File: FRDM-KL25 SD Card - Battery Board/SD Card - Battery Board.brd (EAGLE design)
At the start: 81.3 x 53.3 mm, 64 parts, among them J3 SSW-108-02-S-D, J4 SSW-110-02-S-D, J5 SSW-108-02-S-D, J6 SSW-106-02-S-D, U1 TPS63001, U2 TPS63002, U3 BQ27510DRZT-G3, U4 BQ24210DQCT

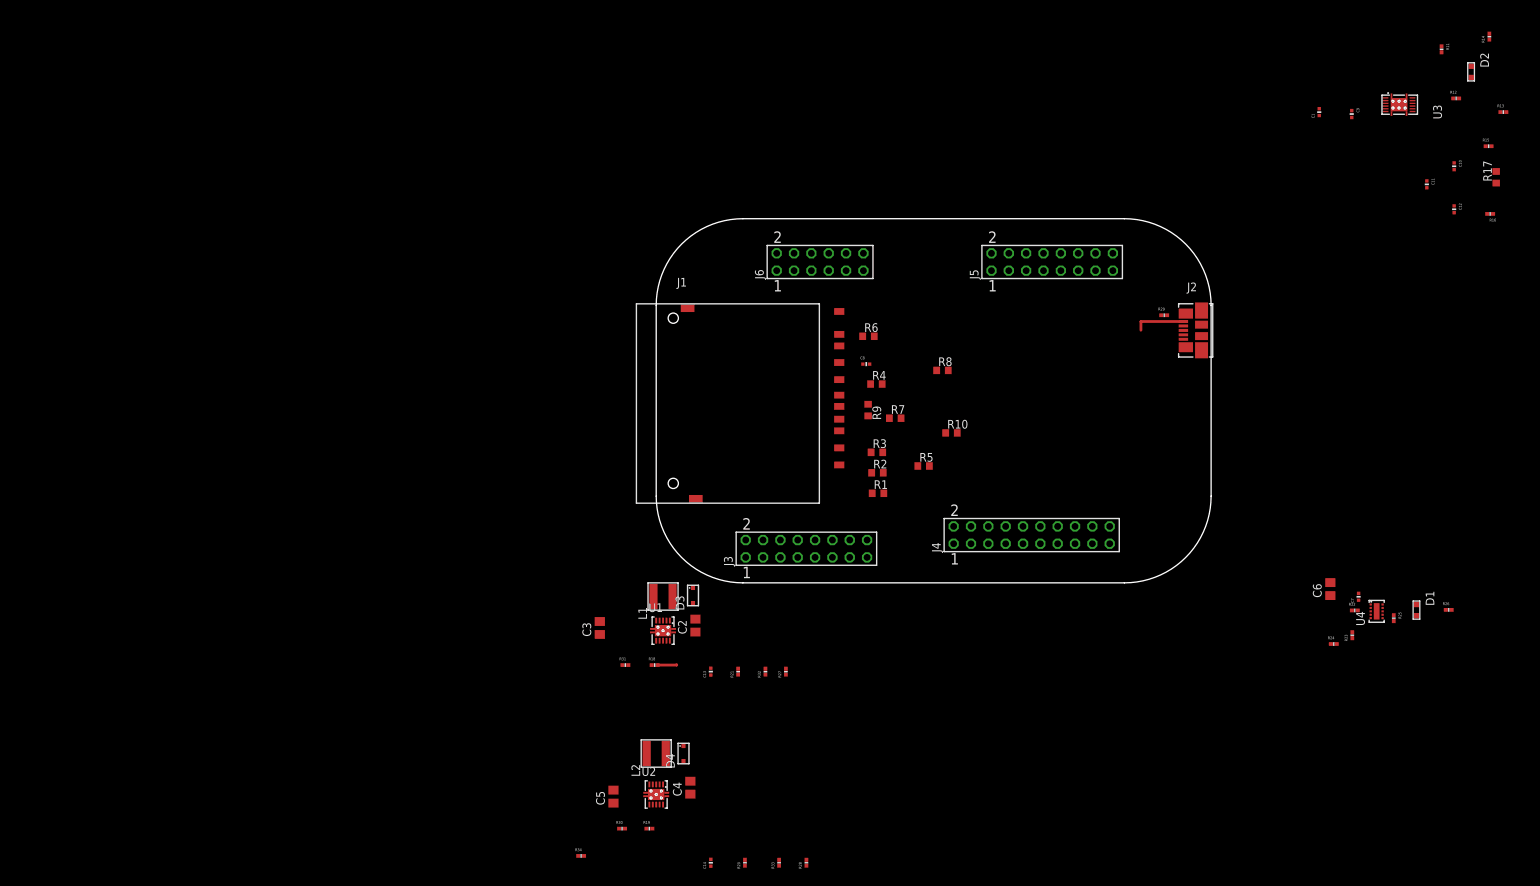
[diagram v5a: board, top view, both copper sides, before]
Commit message: FRDM-KL25Z: Grouped and positioned componets now that all are using 0402 corrected packages to be 0402 and rearanged compoinets to better fit space allowed by the PCB
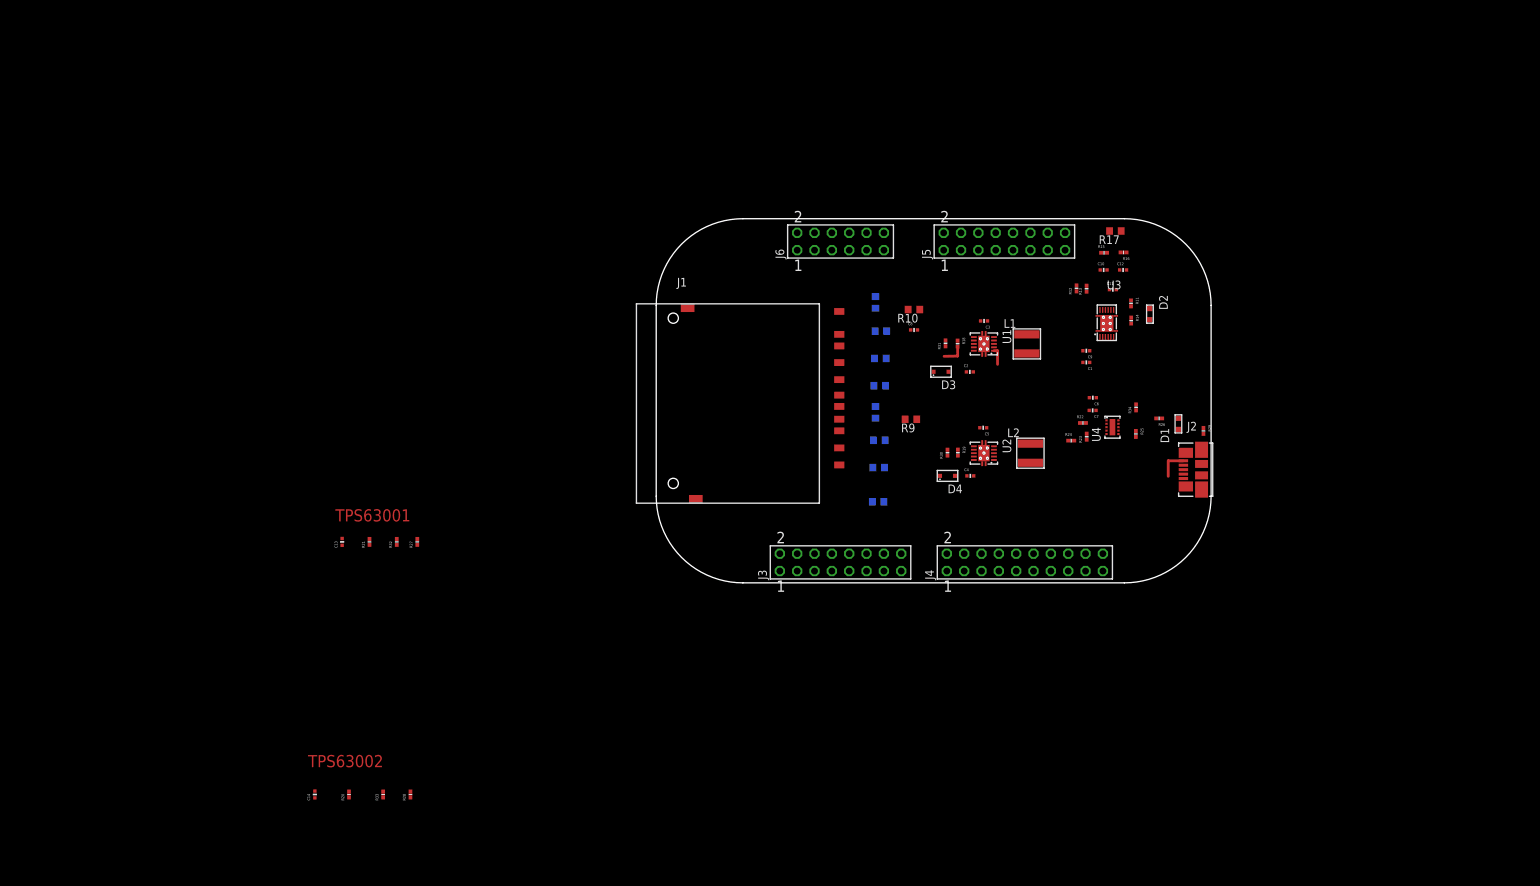
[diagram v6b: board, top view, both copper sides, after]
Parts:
- C2, C3, C4, C5, C6: device Kas-Capacitors:C0805 -> Kas-Capacitors:C0402
- moved R34 104.5 mm to (70.3, 25.7), turned to 90 degrees
- moved C5 76.5 mm to (47.9, 22.7), turned to 180 degrees
- moved R30 72.8 mm to (42.7, 19.1), turned to 90 degrees
- moved C3 72.0 mm to (48.0, 38.4), turned to 180 degrees
- moved R19 71.2 mm to (44.2, 19.1), turned to 270 degrees
- moved L2 70.3 mm to (54.8, 19.0), turned to 180 degrees
- moved U2 69.3 mm to (48.0, 19.0), turned to 90 degrees
- moved R14 67.0 mm to (69.6, 38.4), turned to 270 degrees
- moved R31 66.5 mm to (42.4, 35.1), turned to 90 degrees
- moved R13 66.3 mm to (63.0, 43.1), turned to 90 degrees
- moved L1 64.9 mm to (54.3, 35.0), turned to 180 degrees
- moved R18 64.7 mm to (44.1, 35.0), turned to 270 degrees
- moved U1 63.0 mm to (48.0, 35.0), turned to 90 degrees
- moved R12 62.2 mm to (61.6, 43.1), turned to 90 degrees
- moved C4 61.4 mm to (46.0, 15.7), turned to 0 degrees
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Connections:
- removed net N$12: C5.1, U2.P$5
- net GND: now also R29.1
- net N$28: now also J2.P$11; no longer J2.P$6
- net PACK+: now also C5.1, U2.P$5
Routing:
- net GND: track 7.50 -> 4.50 mm
- net VCC: track 0.00 -> 2.52 mm
- net PACK+: track 2.84 -> 3.41 mm
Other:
- board text added: "TPS63001"
- board text added: "TPS63002"

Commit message: FRDM-KL25Z: Fixed baord outline to matxh with Freescales coordinate system. Placed connectors as per Freescales placement file and replaced all previous components on board in the correct orientation. On the schematics the USB connetor was moved from sheet 2 to sheet 3 with all the other connectors.
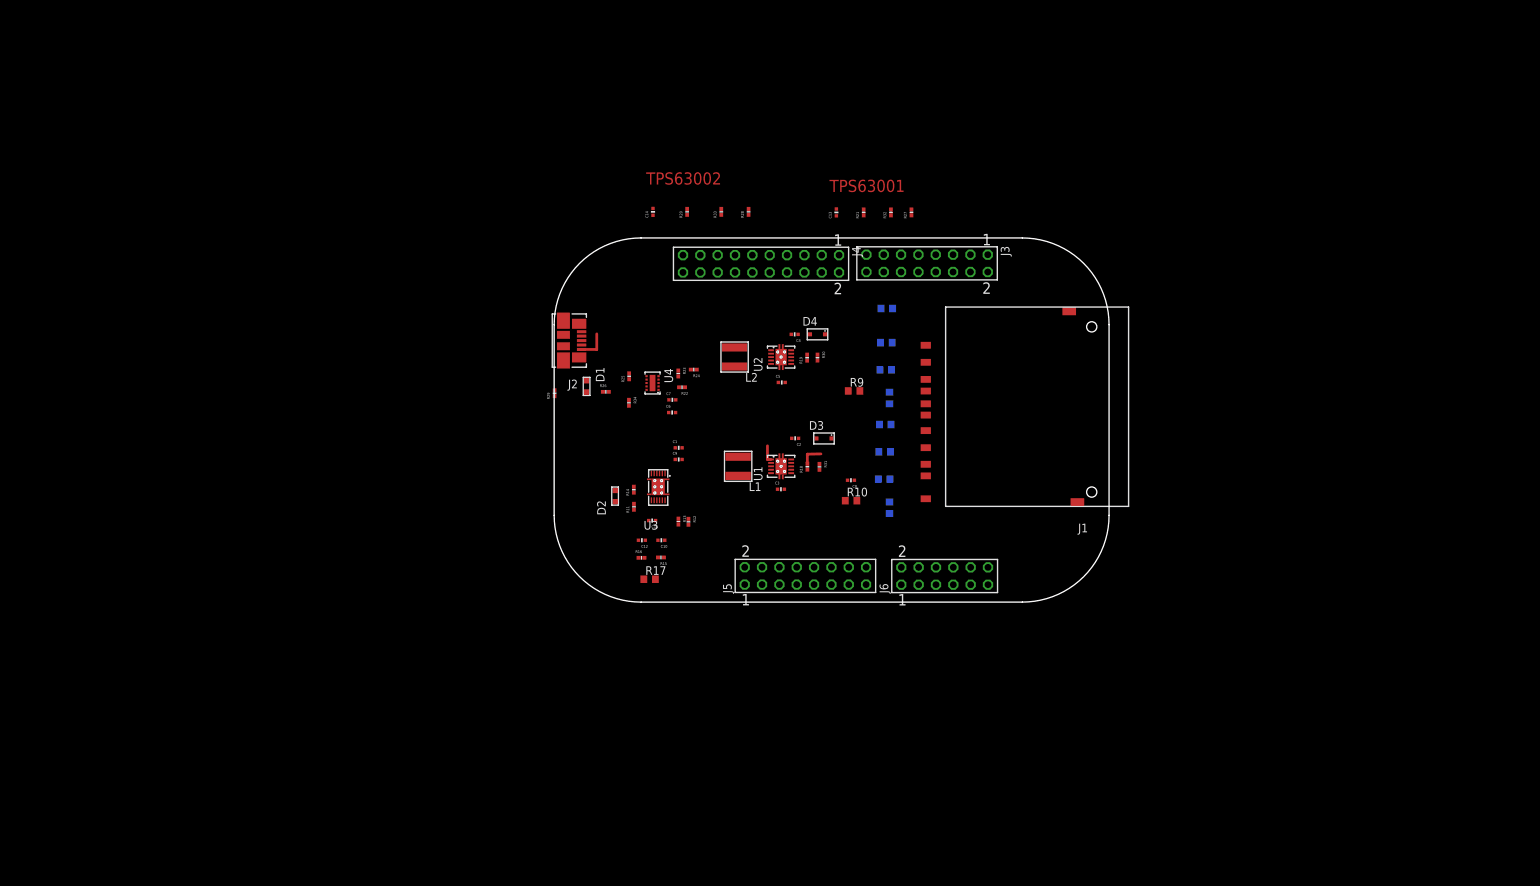
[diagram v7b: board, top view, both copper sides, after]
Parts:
- moved C14 98.7 mm to (-0.47, 54.3)
- moved R20 98.7 mm to (4.53, 54.3)
- moved R28 98.7 mm to (13.5, 54.3)
- moved R33 98.7 mm to (9.53, 54.3)
- moved R29 95.2 mm to (-14.9, 27.8), turned to 90 degrees
- moved J2 90.2 mm to (-10.9, 35.5), turned to 0 degrees
- moved C13 87.0 mm to (26.4, 54.3)
- moved R21 87.0 mm to (30.4, 54.3)
- moved R27 87.0 mm to (37.4, 54.3)
- moved R32 87.0 mm to (34.4, 54.3)
- moved D1 86.9 mm to (-10.2, 28.8), turned to 90 degrees
- moved R17 85.2 mm to (-0.97, 0.53), turned to 0 degrees
- moved R16 83.6 mm to (-2.16, 3.67), turned to 0 degrees
- moved D2 82.8 mm to (-6.03, 12.7), turned to 270 degrees
- moved R26 81.1 mm to (-7.38, 28.0), turned to 0 degrees
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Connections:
- net 3.3V++: now also J5.4, J5.8; no longer J5.3, J5.7
- net 5V++: now also J5.10; no longer J5.9
- net GND: now also J5.12, J5.14; no longer J5.11, J5.13
- net I2C-SCL-0: now also J3.3; no longer J3.4
- net I2C-SCL-1.1: now also J3.4; no longer J3.3
- net I2C-SDA-0: now also J3.1; no longer J3.2
- net I2C-SDA-1.1: now also J3.2; no longer J3.1
- net INT1-21002: now also J3.5; no longer J3.6
- net INT1-8700: now also J3.11; no longer J3.12
- net INT2-8700: now also J3.7; no longer J3.8
- net SPI-MISO-0.1: now also J3.16; no longer J3.15
- net SPI-MOSI-0.1: now also J3.6; no longer J3.5
- net SPI-SCK-0.1: now also J3.8; no longer J3.7
- net VIN: now also J5.16; no longer J5.15

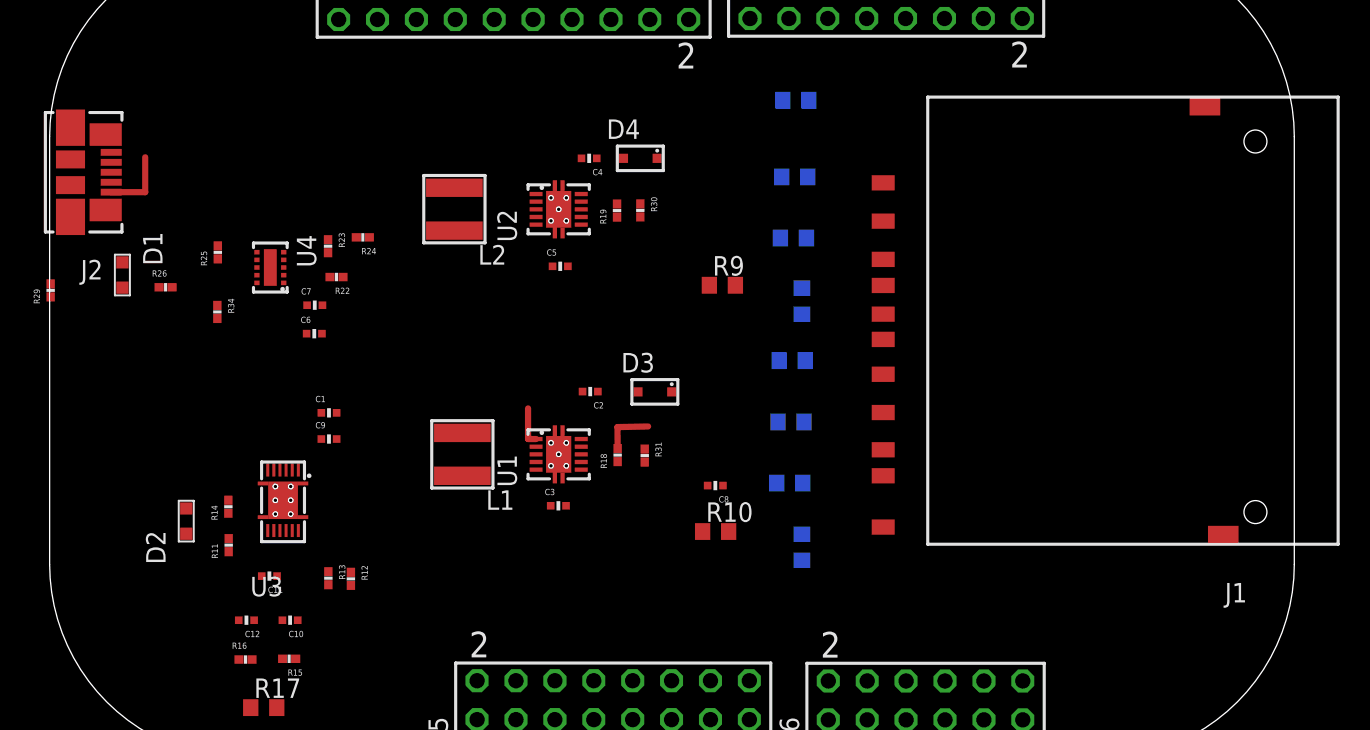
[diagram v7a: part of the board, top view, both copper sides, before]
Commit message: FRDM-KL25Z: LED names were updated to refelect the correct color, Layout of page 3 schematics was rearranged for better clarity. The the PCB the location of the SD card was placed in teh center, USB receptical was also placed in its needed location, SD card pull up resistors have been placed and connected, vias with 0.1 inch spacing have been used to ficilitate a header or test pins should that be needed.
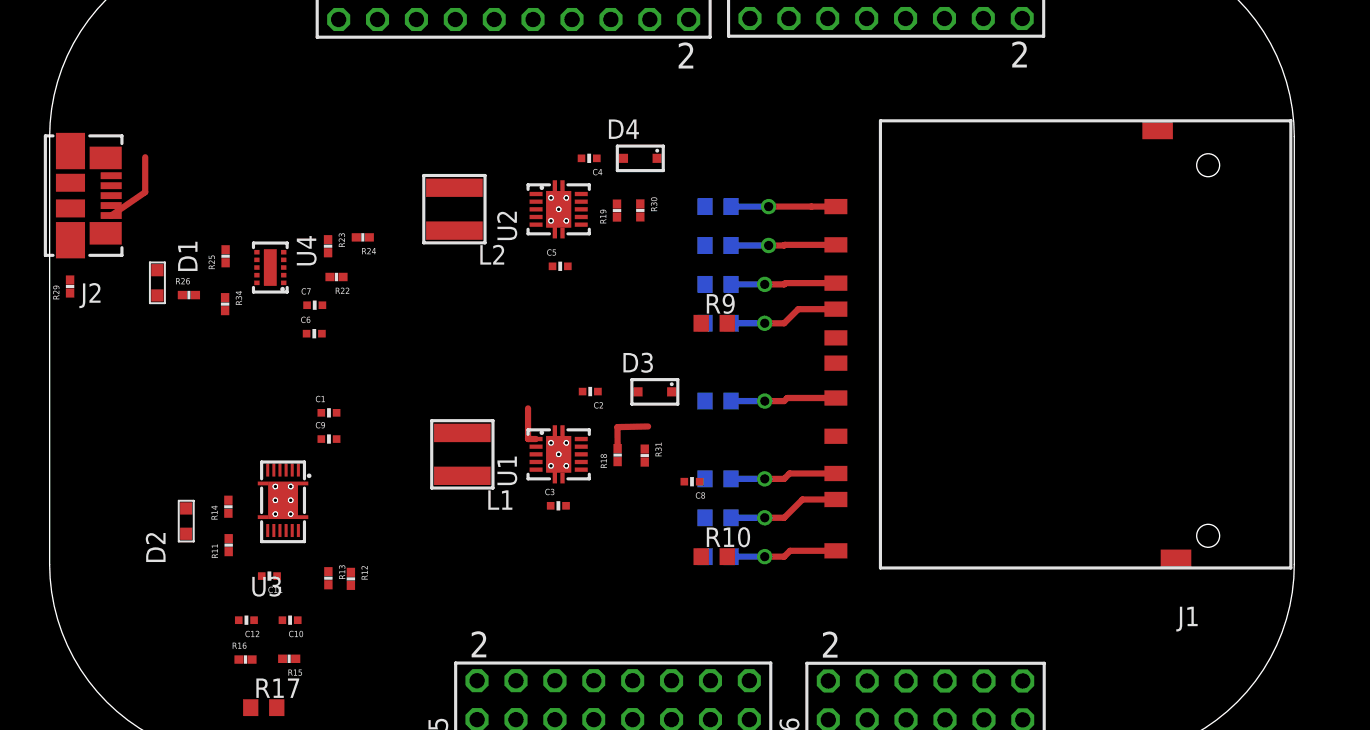
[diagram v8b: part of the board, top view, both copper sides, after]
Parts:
- D1: value Blue-LED -> Red-LED
- D2: value Green-LED -> Yellow-LED
- moved R1 8.60 mm to (28.7, 33.2)
- moved R2 6.72 mm to (28.7, 30.7)
- moved R5 6.04 mm to (28.7, 15.5)
- moved R3 5.78 mm to (28.7, 28.2)
- moved R7 5.66 mm to (28.7, 25.6), turned to 0 degrees
- moved R4 5.52 mm to (28.7, 20.5)
- moved R8 5.51 mm to (28.7, 10.4), turned to 0 degrees
- moved R6 5.20 mm to (28.7, 12.9)
- moved J1 3.45 mm to (60.7, 23.9)
- moved R9 2.54 mm to (28.4, 25.6)
- moved D1 2.34 mm to (-7.91, 28.3)
- moved R10 1.64 mm to (28.4, 10.4)
- moved R26 1.61 mm to (-5.85, 27.5)
- moved C8 1.55 mm to (27.0, 15.3)
- moved J2 1.52 mm to (-10.9, 34.0)
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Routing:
- net N$25: track 0.00 -> 7.34 mm, vias 0 -> 1
- net N$19: track 0.00 -> 7.23 mm, vias 0 -> 1
- net N$26: track 0.00 -> 7.00 mm, vias 0 -> 1
- net SPI-MISO: track 0.00 -> 6.99 mm, vias 0 -> 1
- net SPI-SCLK: track 0.00 -> 6.93 mm, vias 0 -> 1
- net SPI-MOSI: track 0.00 -> 6.88 mm, vias 0 -> 1
- net SPI-CSB-SD: track 0.00 -> 6.86 mm, vias 0 -> 1
- net N$16: track 0.00 -> 6.84 mm, vias 0 -> 1
